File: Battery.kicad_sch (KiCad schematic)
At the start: 56 parts, among them J10 Battery, J9 USB_C_Receptacle_USB2.0_14P, Q1 AON7544, Q2 AON7544, SW2 SW_Push_DPDT, U5 CH224Q, U6 TP5100, U7 TPS54620RHLR

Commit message: hardware: update design and tapeout for fabrication
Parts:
- removed Q1, Q2: AON7544, Package_SO:Vishay_PowerPAK_1212-8_Single, symbol Transistor_FET:BSC026N08NS5
- added Q1, Q2: AON7407, RM_Guided_Dart_Base_HW-Footprints:Vishay_PowerPAK_1212-8_Single, symbol RM_Guided_Dart_Base_HW:AON6411
- C11, C13, C14, C15, C22, C23, C27, C28: footprint Capacitor_SMD:C_0603_1608Metric -> RM_Guided_Dart_Base_HW-Footprints:C_0603_1608Metric; symbol Device:C -> RM_Guided_Dart_Base_HW:C
- C12, C16, C17, C18, C19, C20, C21, C24, C25, C26, C30: footprint Capacitor_SMD:C_0402_1005Metric -> RM_Guided_Dart_Base_HW-Footprints:C_0402_1005Metric; symbol Device:C -> RM_Guided_Dart_Base_HW:C
- C29, C47: footprint Capacitor_SMD:C_1206_3216Metric -> RM_Guided_Dart_Base_HW-Footprints:C_1206_3216Metric; symbol Device:C -> RM_Guided_Dart_Base_HW:C
- D2, D3, D4, D5: footprint LED_SMD:LED_0402_1005Metric -> RM_Guided_Dart_Base_HW-Footprints:LED_0402_1005Metric; symbol Device:LED -> RM_Guided_Dart_Base_HW:LED
- D6, D7: footprint Diode_SMD:D_SMA -> RM_Guided_Dart_Base_HW-Footprints:D_SMA; symbol Diode:SS34 -> RM_Guided_Dart_Base_HW:SS34
- D8: footprint Diode_SMD:D_SOD-323 -> RM_Guided_Dart_Base_HW-Footprints:D_SOD-323; symbol Library:D_Zener -> RM_Guided_Dart_Base_HW:D_Zener
- J10: footprint RWN_Footprints:AMASS_XT30APW-M_1x02_P2.50mm_Horizontal -> RM_Guided_Dart_Base_HW-Footprints:AMASS_XT30APW-M_1x02_P2.50mm_Horizontal; symbol Connector_Generic:Conn_01x02 -> RM_Guided_Dart_Base_HW:Conn_01x02
- J9: footprint RWN_Footprints:USB-C-TH_KH-TYPE-C-W-16P-T -> RM_Guided_Dart_Base_HW-Footprints:USB-C-TH_KH-TYPE-C-W-16P-T; symbol Connector:USB_C_Receptacle_USB2.0_14P -> RM_Guided_Dart_Base_HW:USB_C_Receptacle_USB2.0_14P
- L3, L4: footprint Inductor_SMD:L_APV_APH0630 -> RM_Guided_Dart_Base_HW-Footprints:L_APV_APH0630; symbol Device:L -> RM_Guided_Dart_Base_HW:L
- R14, R15, R16, R17, R18, R19, R20, R21, R24, R25, R27, R28, R29, R30, R31: footprint Resistor_SMD:R_0402_1005Metric -> RM_Guided_Dart_Base_HW-Footprints:R_0402_1005Metric; symbol Device:R -> RM_Guided_Dart_Base_HW:R
- R22, R23, R26: footprint Resistor_SMD:R_0805_2012Metric -> RM_Guided_Dart_Base_HW-Footprints:R_0805_2012Metric; symbol Device:R -> RM_Guided_Dart_Base_HW:R
- SW2: footprint Button_Switch_THT:SW_E-Switch_EG1271_SPDT -> RM_Guided_Dart_Base_HW-Footprints:SW_E-Switch_EG1271_SPDT; symbol Switch:SW_Push_DPDT -> RM_Guided_Dart_Base_HW:SW_Push_DPDT
- U5: footprint RWN_Footprints:DFN-10-1EP_2x2mm_P0.4mm_EP0.9x1.5mm -> RM_Guided_Dart_Base_HW-Footprints:DFN-10-1EP_2x2mm_P0.4mm_EP0.9x1.5mm; symbol RWN_Symbols:CH224Q -> RM_Guided_Dart_Base_HW:CH224Q_1
- U6: footprint Package_DFN_QFN:QFN-16-1EP_4x4mm_P0.65mm_EP2.1x2.1mm_ThermalVias -> RM_Guided_Dart_Base_HW-Footprints:QFN-16-1EP_4x4mm_P0.65mm_EP2.1x2.1mm_ThermalVias; symbol RWN_Symbols:TP5100 -> RM_Guided_Dart_Base_HW:TP5100_1
- U7: footprint RWN_Footprints:VQFN-14_L3.5-W3.5-P0.50-TL-EP_TPS54620RHLR -> RM_Guided_Dart_Base_HW-Footprints:VQFN-14_L3.5-W3.5-P0.50-TL-EP_TPS54620RHLR; symbol RWN_Symbols:TPS54620RHLR -> RM_Guided_Dart_Base_HW:TPS54620RHLR_1
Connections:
- net Battery_Power: now also Q2.5 (D)
- net Power_IN: now also Q1.1 (S), Q1.2 (S), Q1.3 (S), Q2.1 (S), Q2.2 (S), Q2.3 (S)
- net TypeC_Power: now also Q1.5 (D)
- net at C14.2, C17.2, R16.1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: now also Q2.4 (G)
- net at U6.6 (PWR_ON-): now also Q1.4 (G)

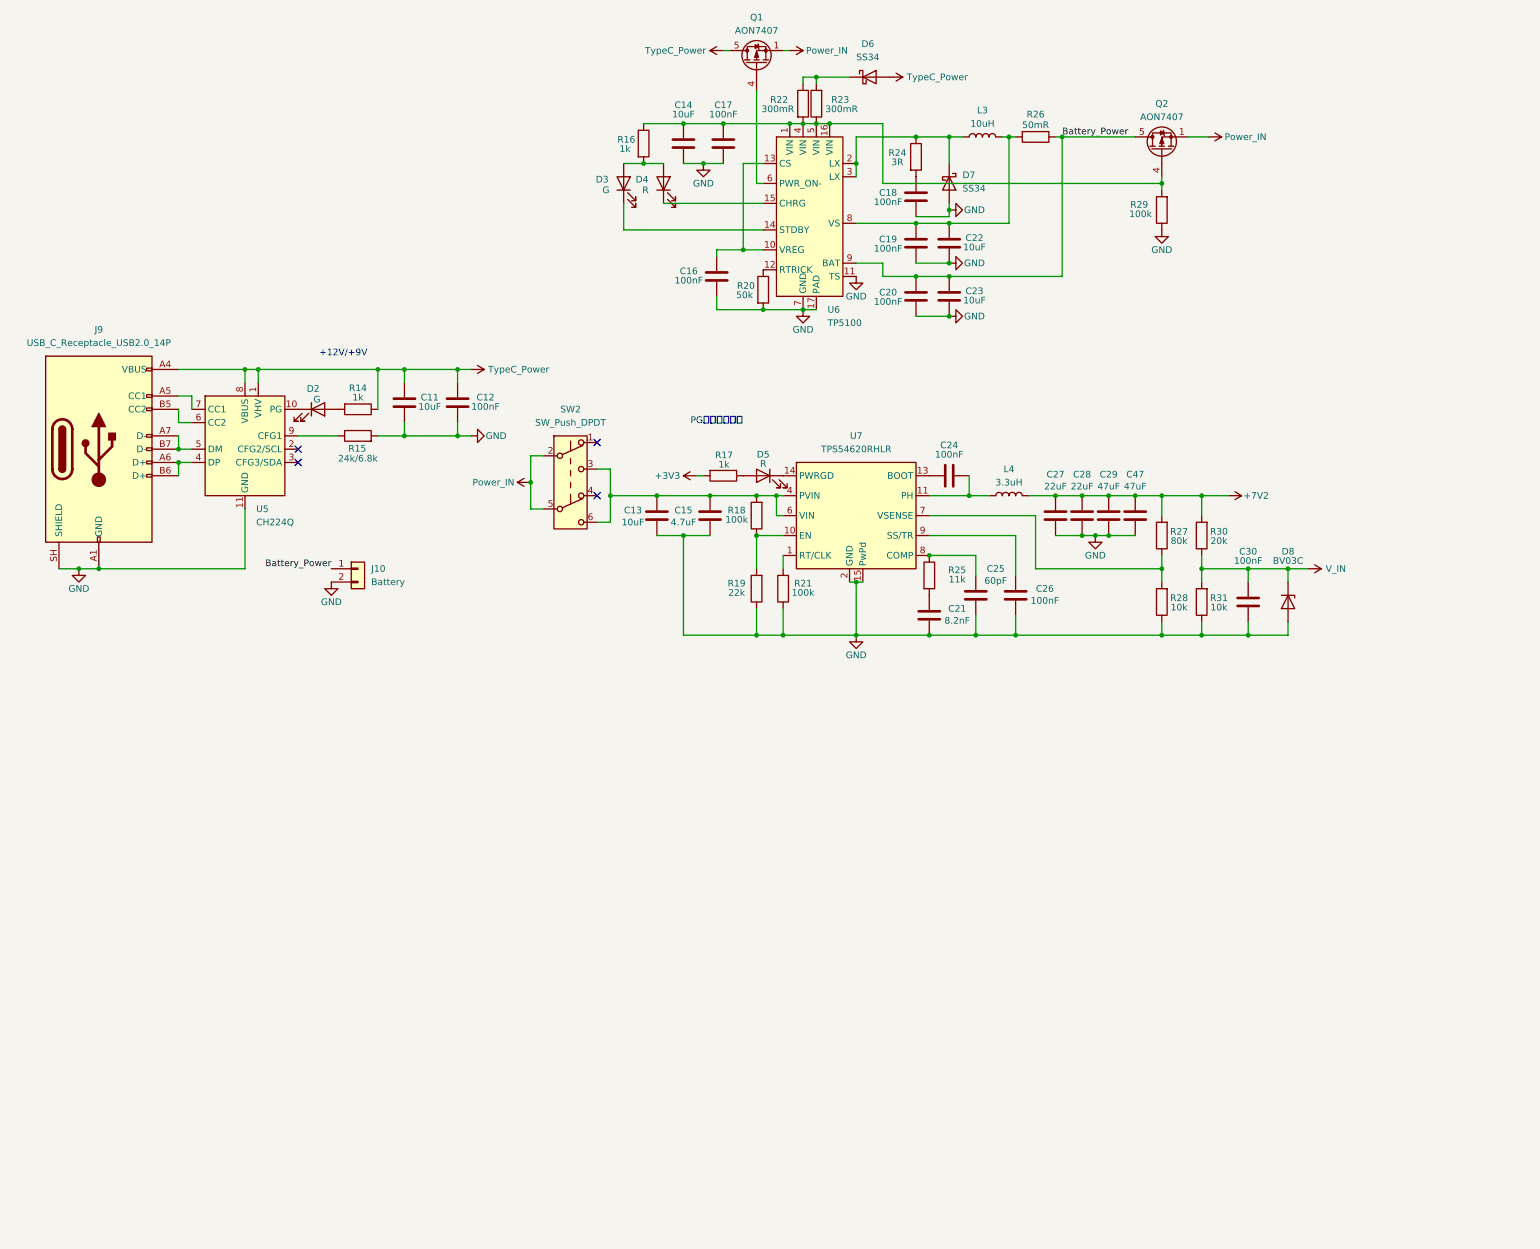
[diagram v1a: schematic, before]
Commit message: V1.2已打板
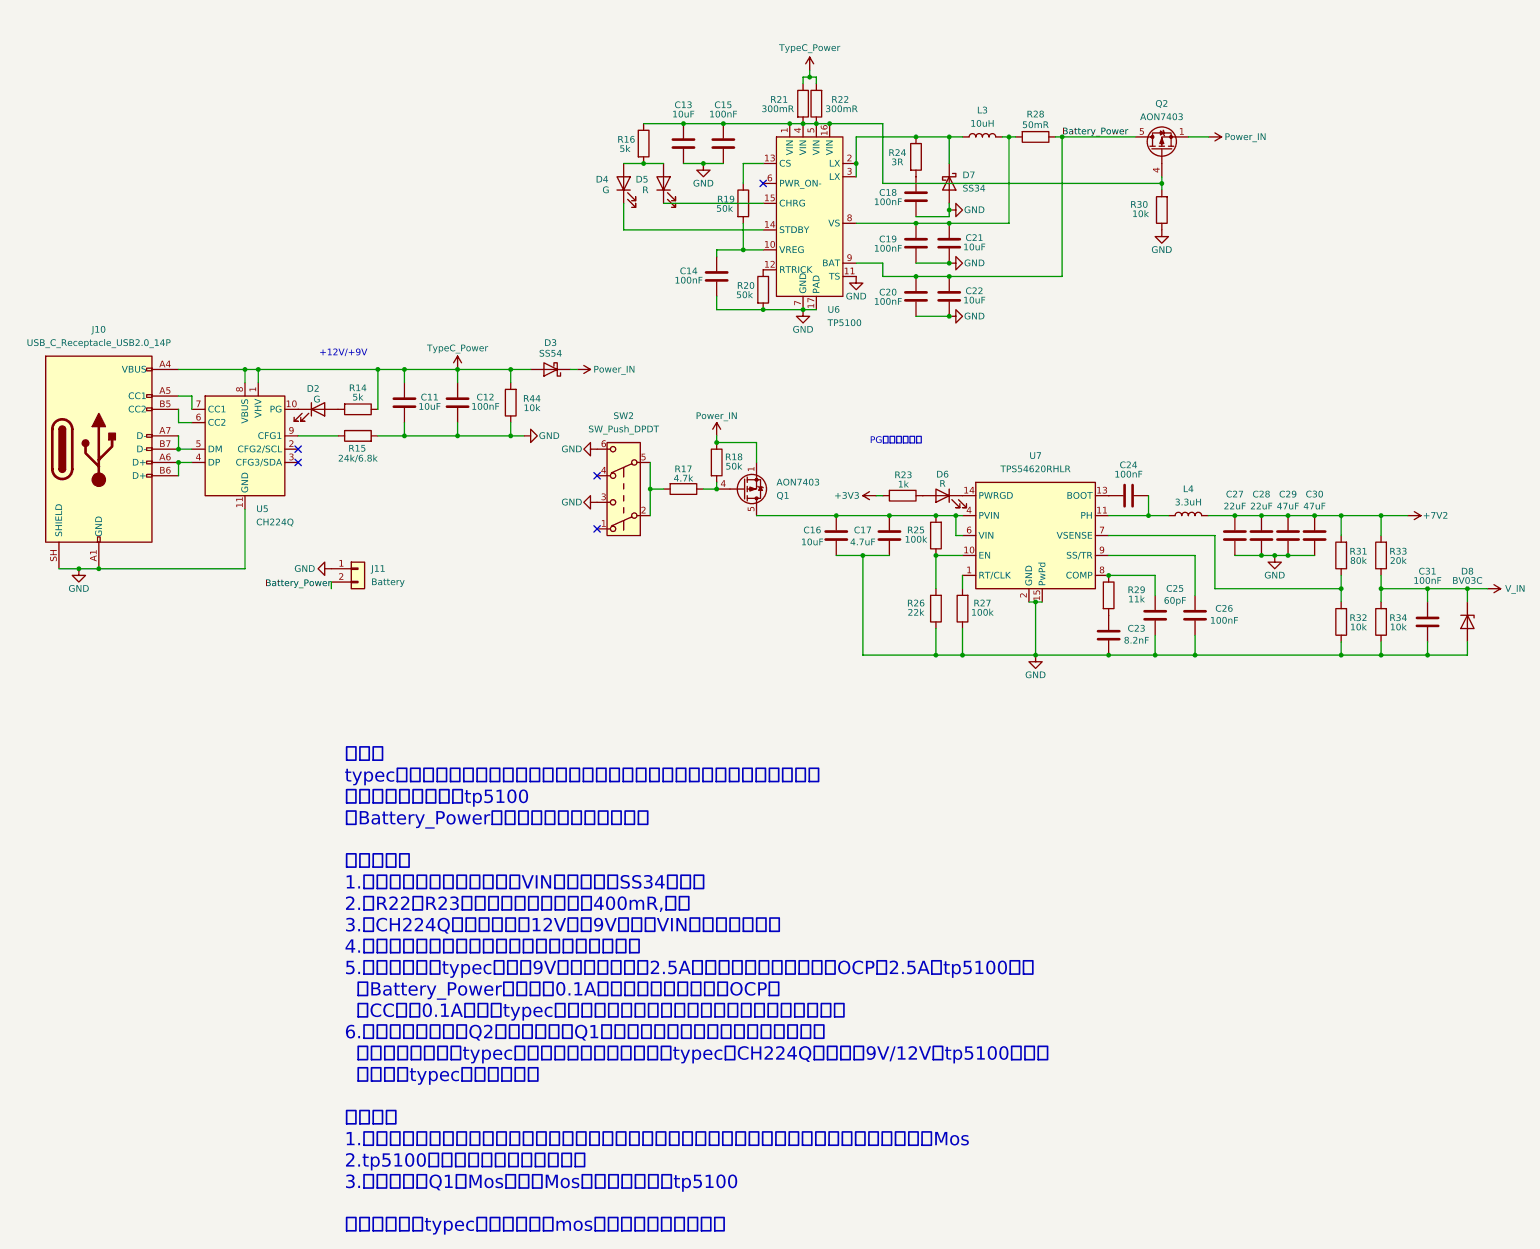
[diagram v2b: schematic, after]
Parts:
- removed D6: SS34, RM_Guided_Dart_Base_HW-Footprints:D_SMA, symbol RM_Guided_Dart_Base_HW:SS34
- added D3: SS54, RM_Guided_Dart_Base_HW-Footprints:D_SMA, symbol RM_Guided_Dart_Base_HW:SS34
- added R17: 4.7k, RM_Guided_Dart_Base_HW-Footprints:R_0402_1005Metric, symbol RM_Guided_Dart_Base_HW:R
- added R18, R19: 50k, RM_Guided_Dart_Base_HW-Footprints:R_0402_1005Metric, symbol RM_Guided_Dart_Base_HW:R
- added R44: 10k, RM_Guided_Dart_Base_HW-Footprints:R_0402_1005Metric, symbol RM_Guided_Dart_Base_HW:R
- Q1, Q2: value AON7407 -> AON7403; footprint RM_Guided_Dart_Base_HW-Footprints:Vishay_PowerPAK_1212-8_Single -> Package_SO:Vishay_PowerPAK_1212-8_Single
- R14, R16: value 1k -> 5k
- R30: renamed from R29; value 100k -> 10k
- renumbered C14 to C13, C16 to C14, C17 to C15, C13 to C16, C15 to C17, C22 to C21, C23 to C22, C21 to C23, C47 to C30, C30 to C31, D3 to D4, D4 to D5, D5 to D6, J9 to J10, J10 to J11, R22 to R21, R23 to R22, R17 to R23, R18 to R25, R19 to R26, R21 to R27, R26 to R28, R25 to R29, R27 to R31, R28 to R32, R30 to R33, R31 to R34
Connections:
- net Battery_Power: now also J11.2 (Pin_2); no longer J11.1 (Pin_1)
- net GND: now also J11.1 (Pin_1), SW2.3 (C), SW2.6 (C), R44.1; no longer J11.2 (Pin_2)
- net Power_IN: now also D3.1 (K), R18.1; no longer SW2.2 (B), SW2.5 (B)
- net TypeC_Power: now also R21.1, R22.2, D3.2 (A), R44.2; no longer Q1.5 (D)
- net at C14.2, U6.10 (VREG): now also R19.2; no longer U6.13 (CS)
- net at Q1.4 (G): now also R17.1, R18.2; no longer U6.6 (PWR_ON-)
- net at C16.1, C17.1, R25.2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: now also Q1.5 (D); no longer SW2.3 (C), SW2.6 (C)
- new net: R17.2, SW2.2 (B), SW2.5 (B)
- new net: R19.1, U6.13 (CS)
- no-connect marks 4 -> 5
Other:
- note added: "问题： typec输入时开关无论处在开或关都能正常上电，后级降压稳定，无静态功耗， 但切换时会瞬间烧掉tp5100 从Battery_Power处供电，开关切换一切正常 排查过程： 1.怀疑切换瞬间有倒灌电流使VIN升压，去掉SS34，无果 2.将R22和R23换成和数据手册一样的400mR,无果 3.将CH224Q的诱骗电压从12V降到9V以远离VIN电压上限，无果 4.怀疑开关瞬间后级电容充电大电流，去掉后无果 5.用数字电源在typec处上电9V一切正常，限流2.5A以下开关切换瞬间都会进OCP，2.5A后tp5100烧毁 在Battery_Power处上电用0.1A限流开关切换都不会进OCP。 用CC模式0.1A限流在typec上电，开关切换会有一秒左右的掉压，后恢复正常 6.怀疑电流倒灌去掉Q2，无果。去掉Q1后短接漏极源极，开关切换恢复正常。 但因为挂载电池时typec输入也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"
- moved on the sheet: C16, C17, C23, C24, C25, C26, C27, C28, C29, C30, C31, D6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
